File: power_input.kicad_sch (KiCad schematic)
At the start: 2 parts, among them J5 Barrel_Jack

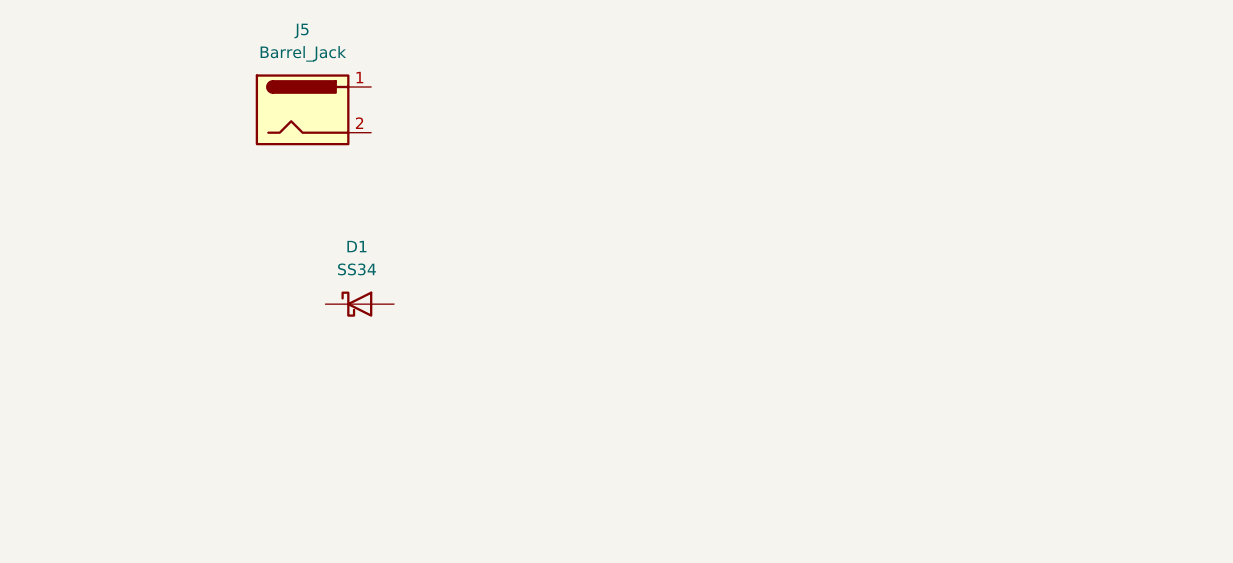
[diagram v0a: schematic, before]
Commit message: adding hierachical sheets: Isolated circuits, esp32, etc
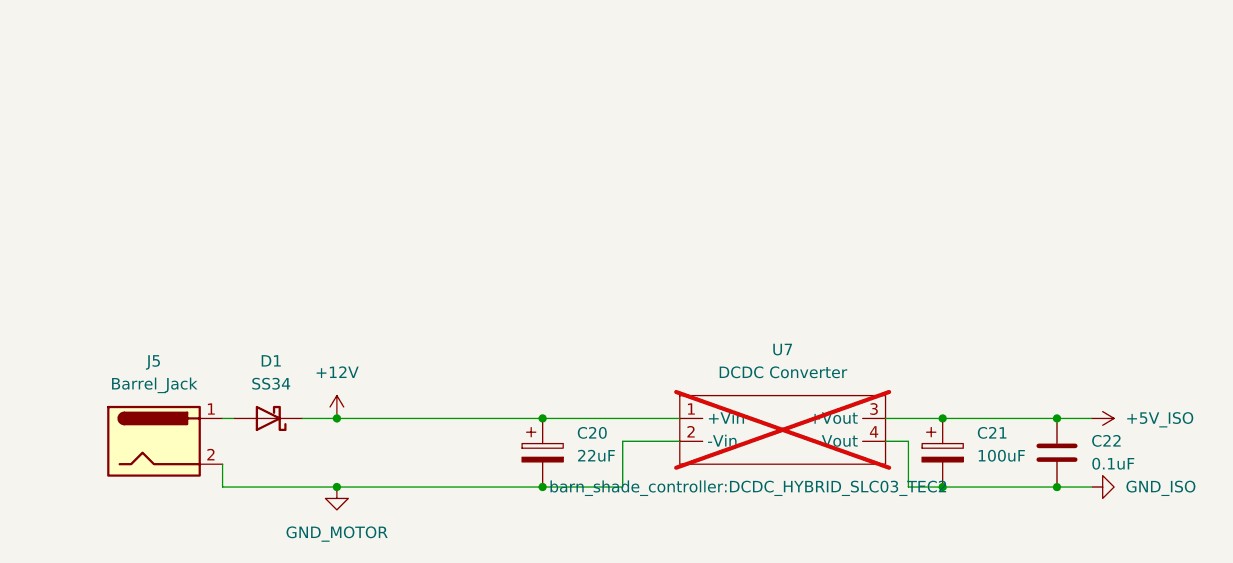
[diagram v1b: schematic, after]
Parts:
- added C20: 22uF, symbol Device:C_Polarized
- added C21: 100uF, symbol Device:C_Polarized
- added C22: 0.1uF, symbol Device:C
- added U7: DCDC Converter, barn_shade_controller:DCDC_HYBRID_SLC03_TEC2, symbol New_Library:DCDC_HYBRID_SLC03_TEC2
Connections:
- net +12V: now reaches D1.1 (K)
- net +12V: now also C20.1, U7.1 (+Vin)
- net at D1.2 (A): now also J5.1
- net GND_MOTOR: now reaches J5.2
- net GND_MOTOR: now also C20.2, U7.2 (-Vin)
- new net +5V_ISO: C21.1, C22.1, U7.3 (+Vout)
- new net GND_ISO: C21.2, C22.2, U7.4 (-Vout)
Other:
- moved on the sheet: D1, J5

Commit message: Started running traces
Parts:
- C20: footprint (none) -> Capacitor_SMD:C_0805_2012Metric
- C21: footprint (none) -> Capacitor_SMD:CP_Elec_6.3x5.4
- C22: footprint (none) -> Capacitor_SMD:C_0603_1608Metric
- J1: renamed from J5; value Barrel_Jack -> DC005-T25; footprint (none) -> Connector_BarrelJack:BarrelJack_Horizontal
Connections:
- net +12V renamed +12V_RAW
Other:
- moved on the sheet: C20
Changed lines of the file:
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@@
+	)
+	(junction
+		(at 124.46 82.55)
+		(diameter 0)
+		(color 0 0 0 0)
 	)
 	(junction
@@
 	)
 	(junction
-		(at 128.27 74.93)
-		(diameter 0)
-		(color 0 0 0 0)
-	)
-	(junction
-		(at 128.27 82.55)
-		(diameter 0)
-		(color 0 0 0 0)
-	)
-	(junction
 		(at 105.41 82.55)
 		(diameter 0)
 		(color 0 0 0 0)
 	)
+	(junction
+		(at 124.46 74.93)
+		(diameter 0)
+		(color 0 0 0 0)
+	)
 	(wire
 		(pts
@@
 	(wire
 		(pts
-			(xy 105.41 82.55) (xy 128.27 82.55)
+			(xy 105.41 82.55) (xy 124.46 82.55)
 		)
 		(stroke
@@
 	(wire
 		(pts
-			(xy 105.41 74.93) (xy 128.27 74.93)
+			(xy 124.46 74.93) (xy 143.51 74.93)
+		)
+		(stroke
+			(width 0)
+			(type default)
+		)
+	)
+	(wire
+		(pts
+			(xy 105.41 74.93) (xy 124.46 74.93)
 		)
 		(stroke
@@
 	(wire
 		(pts
-			(xy 128.27 74.93) (xy 143.51 74.93)
+			(xy 124.46 82.55) (xy 137.16 82.55)
 		)
 		(stroke
@@
 		(pts
 			(xy 189.23 82.55) (xy 185.42 82.55)
-		)
-		(stroke
-			(width 0)
-			(type default)
-		)
-	)
-	(wire
-		(pts
-			(xy 128.27 82.55) (xy 137.16 82.55)
 		)
 		(stroke
@@
 	(symbol
 		(lib_id "Device:C_Polarized")
-		(at 128.27 78.74 0)
+		(at 124.46 78.74 0)
 		(unit 1)
 		(exclude_from_sim no)
@@
 		(fields_autoplaced yes)
 		(property "Reference" "C20"
-			(at 132.08 76.5809 0)
+			(at 128.27 76.5809 0)
 			(effects
 				(font
@@
 		)
 		(property "Value" "22uF"
-			(at 132.08 79.1209 0)
+			(at 128.27 79.1209 0)
 			(effects
 				(font
@@
 			)
 		)
-		(property "Footprint" ""
-			(at 129.2352 82.55 0)
+		(property "Footprint" "Capacitor_SMD:C_0805_2012Metric"
+			(at 125.4252 82.55 0)
 			(effects
 				(font
@@
 		)
 		(property "Datasheet" "~"
-			(at 128.27 78.74 0)
+			(at 124.46 78.74 0)
 			(effects
 				(font
@@
 		)
 		(property "Description" "Polarized capacitor"
-			(at 128.27 78.74 0)
+			(at 124.46 78.74 0)
 			(effects
 				(font
@@
 			)
 		)
-		(property "Footprint" ""
+		(property "Footprint" "Capacitor_SMD:C_0603_1608Metric"
 			(at 186.3852 82.55 0)
 			(effects
@@
 			)
 		)
-		(property "Value" "+12V"
+		(property "Value" "+12V_RAW"
 			(at 105.41 69.85 0)
 			(effects
@@
 		(dnp no)
 		(fields_autoplaced yes)
-		(property "Reference" "J5"
+		(property "Reference" "J1"
 			(at 85.09 68.58 0)
 			(effects
@@
 			)
 		)
-		(property "Value" "Barrel_Jack"
+		(property "Value" "DC005-T25"
 			(at 85.09 71.12 0)
 			(effects
@@
 			)
 		)
-		(property "Footprint" ""
+		(property "Footprint" "Connector_BarrelJack:BarrelJack_Horizontal"
 			(at 86.36 78.486 0)
 			(effects
@@
 			(project "barn-blinds-controller"
 				(path "/aa90962a-81b9-423d-8acd-c4e83fa798bb/bb2a80bd-a98d-4040-85a8-f5c2f3802634"
-					(reference "J5")
+					(reference "J1")
 					(unit 1)
 				)
@@
 			)
 		)
-		(property "Footprint" ""
+		(property "Footprint" "Capacitor_SMD:CP_Elec_6.3x5.4"
 			(at 173.6852 82.55 0)
 			(effects

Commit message: BOM work
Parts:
- C1: renamed from C20; LCSC (none) -> C5674
- C2: renamed from C21; LCSC (none) -> C7469977
- C3: renamed from C22; LCSC (none) -> C1590
- D1: LCSC (none) -> C8678
- J1: LCSC (none) -> C111573
- U1: renamed from U7; LCSC (none) -> C5899332
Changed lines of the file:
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@@
 		(dnp no)
 		(fields_autoplaced yes)
-		(property "Reference" "#PWR035"
+		(property "Reference" "#PWR03"
 			(at 185.42 74.93 0)
 			(effects
@@
 			(project "barn-blinds-controller"
 				(path "/aa90962a-81b9-423d-8acd-c4e83fa798bb/bb2a80bd-a98d-4040-85a8-f5c2f3802634"
-					(reference "#PWR035")
+					(reference "#PWR03")
 					(unit 1)
 				)
@@
 		(dnp no)
 		(fields_autoplaced yes)
-		(property "Reference" "C20"
+		(property "Reference" "C1"
 			(at 128.27 76.5809 0)
 			(effects
@@
 			)
 		)
+		(property "LCSC" "C5674"
+			(at 124.46 78.74 0)
+			(effects
+				(font
+					(size 1.27 1.27)
+				)
+				(hide yes)
+			)
+		)
 		(pin "1"
 		)
@@
 			(project "barn-blinds-controller"
 				(path "/aa90962a-81b9-423d-8acd-c4e83fa798bb/bb2a80bd-a98d-4040-85a8-f5c2f3802634"
-					(reference "C20")
+					(reference "C1")
 					(unit 1)
 				)
@@
 		(dnp yes)
 		(fields_autoplaced yes)
-		(property "Reference" "U7"
+		(property "Reference" "U1"
 			(at 154.94 67.31 0)
 			(effects
@@
 			)
 		)
+		(property "LCSC" "C5899332"
+			(at 151.13 82.55 0)
+			(effects
+				(font
+					(size 1.27 1.27)
+				)
+				(hide yes)
+			)
+		)
 		(pin "4"
 		)
@@
 			(project "barn-blinds-controller"
 				(path "/aa90962a-81b9-423d-8acd-c4e83fa798bb/bb2a80bd-a98d-4040-85a8-f5c2f3802634"
-					(reference "U7")
+					(reference "U1")
 					(unit 1)
 				)
@@
 		(dnp no)
 		(fields_autoplaced yes)
-		(property "Reference" "C22"
+		(property "Reference" "C3"
 			(at 189.23 77.4699 0)
 			(effects
@@
 			)
 		)
+		(property "LCSC" "C1590"
+			(at 185.42 78.74 0)
+			(effects
+				(font
+					(size 1.27 1.27)
+				)
+				(hide yes)
+			)
+		)
 		(pin "2"
 		)
@@
 			(project "barn-blinds-controller"
 				(path "/aa90962a-81b9-423d-8acd-c4e83fa798bb/bb2a80bd-a98d-4040-85a8-f5c2f3802634"
-					(reference "C22")
+					(reference "C3")
 					(unit 1)
 				)
@@
 			)
 		)
+		(property "LCSC" "C8678"
+			(at 97.79 74.93 0)
+			(effects
+				(font
+					(size 1.27 1.27)
+				)
+				(hide yes)
+			)
+		)
 		(pin "2"
 		)
@@
 		(on_board yes)
 		(dnp no)
-		(property "Reference" "#PWR032"
+		(property "Reference" "#PWR01"
 			(at 105.41 78.74 0)
 			(effects
@@
 			(project "barn-blinds-controller"
 				(path "/aa90962a-81b9-423d-8acd-c4e83fa798bb/bb2a80bd-a98d-4040-85a8-f5c2f3802634"
-					(reference "#PWR032")
+					(reference "#PWR01")
 					(unit 1)
 				)
@@
 			)
 		)
+		(property "LCSC" "C111573"
+			(at 85.09 77.47 0)
+			(effects
+				(font
+					(size 1.27 1.27)
+				)
+				(hide yes)
+			)
+		)
 		(pin "1"
 		)
@@
 		(dnp no)
 		(fields_autoplaced yes)
-		(property "Reference" "#PWR036"
+		(property "Reference" "#PWR04"
 			(at 195.58 82.55 0)
 			(effects
@@
 			(project "barn-blinds-controller"
 				(path "/aa90962a-81b9-423d-8acd-c4e83fa798bb/bb2a80bd-a98d-4040-85a8-f5c2f3802634"
-					(reference "#PWR036")
+					(reference "#PWR04")
 					(unit 1)
 				)
@@
 		(dnp no)
 		(fields_autoplaced yes)
-		(property "Reference" "#PWR031"
+		(property "Reference" "#PWR02"
 			(at 105.41 88.9 0)
 			(effects
@@
 			(project "barn-blinds-controller"
 				(path "/aa90962a-81b9-423d-8acd-c4e83fa798bb/bb2a80bd-a98d-4040-85a8-f5c2f3802634"
-					(reference "#PWR031")
+					(reference "#PWR02")
 					(unit 1)
 				)
@@
 		(dnp no)
 		(fields_autoplaced yes)
-		(property "Reference" "C21"
+		(property "Reference" "C2"
 			(at 176.53 76.5809 0)
 			(effects
@@
 			)
 		)
+		(property "LCSC" "C7469977"
+			(at 172.72 78.74 0)
+			(effects
+				(font
+					(size 1.27 1.27)
+				)
+				(hide yes)
+			)
+		)
 		(pin "1"
 		)
@@
 			(project "barn-blinds-controller"
 				(path "/aa90962a-81b9-423d-8acd-c4e83fa798bb/bb2a80bd-a98d-4040-85a8-f5c2f3802634"
-					(reference "C21")
-					(unit 1)
-				)
+					(reference "C2")
+					(unit 1)
+				)

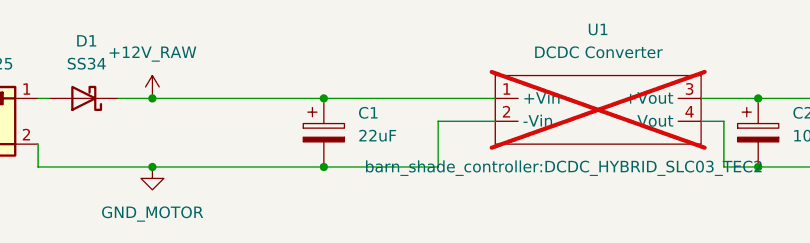
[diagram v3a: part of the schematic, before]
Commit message: Updated BOM, fixed a few components
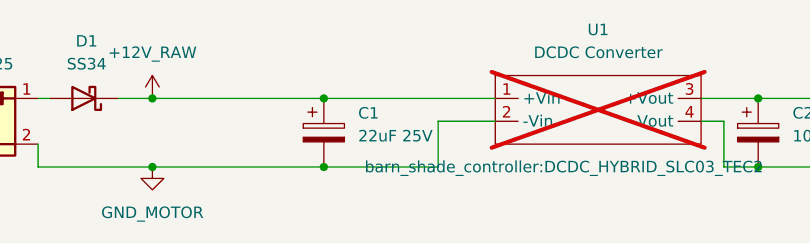
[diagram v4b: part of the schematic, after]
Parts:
- C1: value 22uF -> 22uF 25V; LCSC C5674 -> C45783
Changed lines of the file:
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@@
 			)
 		)
-		(property "Value" "22uF"
+		(property "Value" "22uF 25V"
 			(at 128.27 79.1209 0)
 			(effects
@@
 			)
 		)
-		(property "LCSC" "C5674"
+		(property "LCSC" "C45783"
 			(at 124.46 78.74 0)
 			(effects

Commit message: V 1.2
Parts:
- added TP7: 12V, barn_shade_controller:TestPoint_Pad_D1.0mm_No_SolderMask, symbol Connector:TestPoint
- added TP8: 5V_ISO, barn_shade_controller:TestPoint_Pad_D1.0mm_No_SolderMask, symbol Connector:TestPoint
- J1: value DC005-T25 -> DC005-T20; LCSC C111573 -> C111567
- U1: LCSC C5899332 -> C20622657; now fitted; now in the parts list
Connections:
- net +5V_ISO: now also TP8.1
- net at D1.2 (A), J1.1: now also TP7.1
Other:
- moved on the sheet: J1
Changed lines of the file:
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@@
+	)
+	(junction
+		(at 88.9 74.93)
+		(diameter 0)
+		(color 0 0 0 0)
+	)
+	(junction
+		(at 168.91 74.93)
+		(diameter 0)
+		(color 0 0 0 0)
 	)
 	(junction
@@
 	(wire
 		(pts
+			(xy 88.9 74.93) (xy 83.82 74.93)
+		)
+		(stroke
+			(width 0)
+			(type default)
+		)
+	)
+	(wire
+		(pts
 			(xy 105.41 74.93) (xy 101.6 74.93)
 		)
@@
 	(wire
 		(pts
-			(xy 92.71 82.55) (xy 105.41 82.55)
+			(xy 83.82 82.55) (xy 105.41 82.55)
 		)
 		(stroke
@@
 	(wire
 		(pts
-			(xy 172.72 74.93) (xy 166.37 74.93)
-		)
-		(stroke
-			(width 0)
-			(type default)
-		)
-	)
-	(wire
-		(pts
-			(xy 93.98 74.93) (xy 92.71 74.93)
+			(xy 172.72 74.93) (xy 168.91 74.93)
+		)
+		(stroke
+			(width 0)
+			(type default)
+		)
+	)
+	(wire
+		(pts
+			(xy 93.98 74.93) (xy 88.9 74.93)
 		)
 		(stroke
@@
 	(wire
 		(pts
+			(xy 168.91 74.93) (xy 166.37 74.93)
+		)
+		(stroke
+			(width 0)
+			(type default)
+		)
+	)
+	(wire
+		(pts
 			(xy 124.46 82.55) (xy 137.16 82.55)
 		)
@@
 	(wire
 		(pts
-			(xy 92.71 82.55) (xy 92.71 80.01)
+			(xy 83.82 82.55) (xy 83.82 80.01)
 		)
 		(stroke
@@
 		(unit 1)
 		(exclude_from_sim no)
-		(in_bom no)
-		(on_board yes)
-		(dnp yes)
+		(in_bom yes)
+		(on_board yes)
+		(dnp no)
 		(fields_autoplaced yes)
 		(property "Reference" "U1"
@@
 			)
 		)
-		(property "LCSC" "C5899332"
+		(property "LCSC" "C20622657"
 			(at 151.13 82.55 0)
 			(effects
@@
 	(symbol
 		(lib_id "Connector:Barrel_Jack")
-		(at 85.09 77.47 0)
+		(at 76.2 77.47 0)
 		(unit 1)
 		(exclude_from_sim no)
@@
 		(fields_autoplaced yes)
 		(property "Reference" "J1"
-			(at 85.09 68.58 0)
-			(effects
-				(font
-					(size 1.27 1.27)
-				)
-			)
-		)
-		(property "Value" "DC005-T25"
-			(at 85.09 71.12 0)
+			(at 76.2 68.58 0)
+			(effects
+				(font
+					(size 1.27 1.27)
+				)
+			)
+		)
+		(property "Value" "DC005-T20"
+			(at 76.2 71.12 0)
 			(effects
 				(font
@@
 		)
 		(property "Footprint" "Connector_BarrelJack:BarrelJack_Horizontal"
-			(at 86.36 78.486 0)
+			(at 77.47 78.486 0)
 			(effects
 				(font
@@
 		)
 		(property "Datasheet" "~"
-			(at 86.36 78.486 0)
+			(at 77.47 78.486 0)
 			(effects
 				(font
@@
 		)
 		(property "Description" "DC Barrel Jack"
-			(at 85.09 77.47 0)
-			(effects
-				(font
-					(size 1.27 1.27)
-				)
-				(hide yes)
-			)
-		)
-		(property "LCSC" "C111573"
-			(at 85.09 77.47 0)
+			(at 76.2 77.47 0)
+			(effects
+				(font
+					(size 1.27 1.27)
+				)
+				(hide yes)
+			)
+		)
+		(property "LCSC" "C111567"
+			(at 76.2 77.47 0)
 			(effects
 				(font
@@
 				(path "/aa90962a-81b9-423d-8acd-c4e83fa798bb/bb2a80bd-a98d-4040-85a8-f5c2f3802634"
 					(reference "J1")
+					(unit 1)
+				)
+			)
+		)
+	)
+	(symbol
+		(lib_id "Connector:TestPoint")
+		(at 88.9 74.93 0)
+		(unit 1)
+		(exclude_from_sim no)
+		(in_bom yes)
+		(on_board yes)
+		(dnp no)
+		(fields_autoplaced yes)
+		(property "Reference" "TP7"
+			(at 91.44 70.3579 0)
+			(effects
+				(font
+					(size 1.27 1.27)
+				)
+				(justify left)
+			)
+		)
+		(property "Value" "12V"
+			(at 91.44 72.8979 0)
+			(effects
+				(font
+					(size 1.27 1.27)
+				)
+				(justify left)
+			)
+		)
+		(property "Footprint" "barn_shade_controller:TestPoint_Pad_D1.0mm_No_SolderMask"
+			(at 93.98 74.93 0)
+			(effects
+				(font
+					(size 1.27 1.27)
+				)
+				(hide yes)
+			)
+		)
+		(property "Datasheet" "~"
+			(at 93.98 74.93 0)
+			(effects
+				(font
+					(size 1.27 1.27)
+				)
+				(hide yes)
+			)
+		)
+		(property "Description" "test point"
+			(at 88.9 74.93 0)
+			(effects
+				(font
+					(size 1.27 1.27)
+				)
+				(hide yes)
+			)
+		)
+		(pin "1"
+		)
+		(instances
+			(project "barn-blinds-controller"
+				(path "/aa90962a-81b9-423d-8acd-c4e83fa798bb/bb2a80bd-a98d-4040-85a8-f5c2f3802634"
+					(reference "TP7")
 					(unit 1)
 				)
@@
 					(unit 1)
 				)
+			)
+		)
+	)
+	(symbol
+		(lib_id "Connector:TestPoint")
+		(at 168.91 74.93 0)
+		(unit 1)
+		(exclude_from_sim no)
+		(in_bom yes)
+		(on_board yes)
+		(dnp no)
+		(fields_autoplaced yes)
+		(property "Reference" "TP8"
+			(at 171.45 70.3579 0)
+			(effects
+				(font
+					(size 1.27 1.27)
+				)
+				(justify left)
+			)
+		)
+		(property "Value" "5V_ISO"
+			(at 171.45 72.8979 0)
+			(effects
+				(font
+					(size 1.27 1.27)
+				)
+				(justify left)
+			)
+		)
+		(property "Footprint" "barn_shade_controller:TestPoint_Pad_D1.0mm_No_SolderMask"
+			(at 173.99 74.93 0)
+			(effects
+				(font
+					(size 1.27 1.27)
+				)
+				(hide yes)
+			)
+		)
+		(property "Datasheet" "~"
+			(at 173.99 74.93 0)
+			(effects
+				(font
+					(size 1.27 1.27)
+				)
+				(hide yes)
+			)
+		)
+		(property "Description" "test point"
+			(at 168.91 74.93 0)
+			(effects
+				(font
+					(size 1.27 1.27)
+				)
+				(hide yes)
+			)
+		)
+		(pin "1"
+		)
+		(instances
+			(project "barn-blinds-controller"
+				(path "/aa90962a-81b9-423d-8acd-c4e83fa798bb/bb2a80bd-a98d-4040-85a8-f5c2f3802634"
+					(reference "TP8")
+					(unit 1)
+				)
